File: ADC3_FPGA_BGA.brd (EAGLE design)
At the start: 40.4 x 44.4 mm, 120 parts, among them CON1 MEZZANINE_2X30, CON2 MEZZANINE_2X30, CON3 USB-C, IC1 ARTIX7-FTG256, IC2 3.3V, IC3 2.5V, IC4 MPM3811, IC5 MPM3804, IC6 EEPROM, IC7 93LC56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

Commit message: Create README.md
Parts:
- moved C1 32.8 mm to (23.5, 3.00)
- moved C10 32.8 mm to (17.5, 25.0)
- moved C11 32.8 mm to (2.00, 33.8)
- moved C12 32.8 mm to (21.0, 29.5)
- moved C13 32.8 mm to (23.0, 25.5)
- moved C14 32.8 mm to (17.0, 27.5)
- moved C15 32.8 mm to (21.0, 31.5)
- moved C16 32.8 mm to (20.0, 26.5)
- moved C17 32.8 mm to (23.0, 27.5)
- moved C18 32.8 mm to (19.5, 24.0)
- moved C19 32.8 mm to (13.0, 2.00)
- moved C2 32.8 mm to (17.0, 4.50)
- moved C20 32.8 mm to (7.00, 2.00)
- moved C21 32.8 mm to (22.0, 23.5)
- moved C22 32.8 mm to (19.0, 28.5)
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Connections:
- net DRAM_NRST: now also IC1.D8
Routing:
- net DRAM_NRST: track 1.92 -> 14.0 mm
- net +1V8: track 31.0 -> 31.6 mm
- net GND: vias 168 -> 180

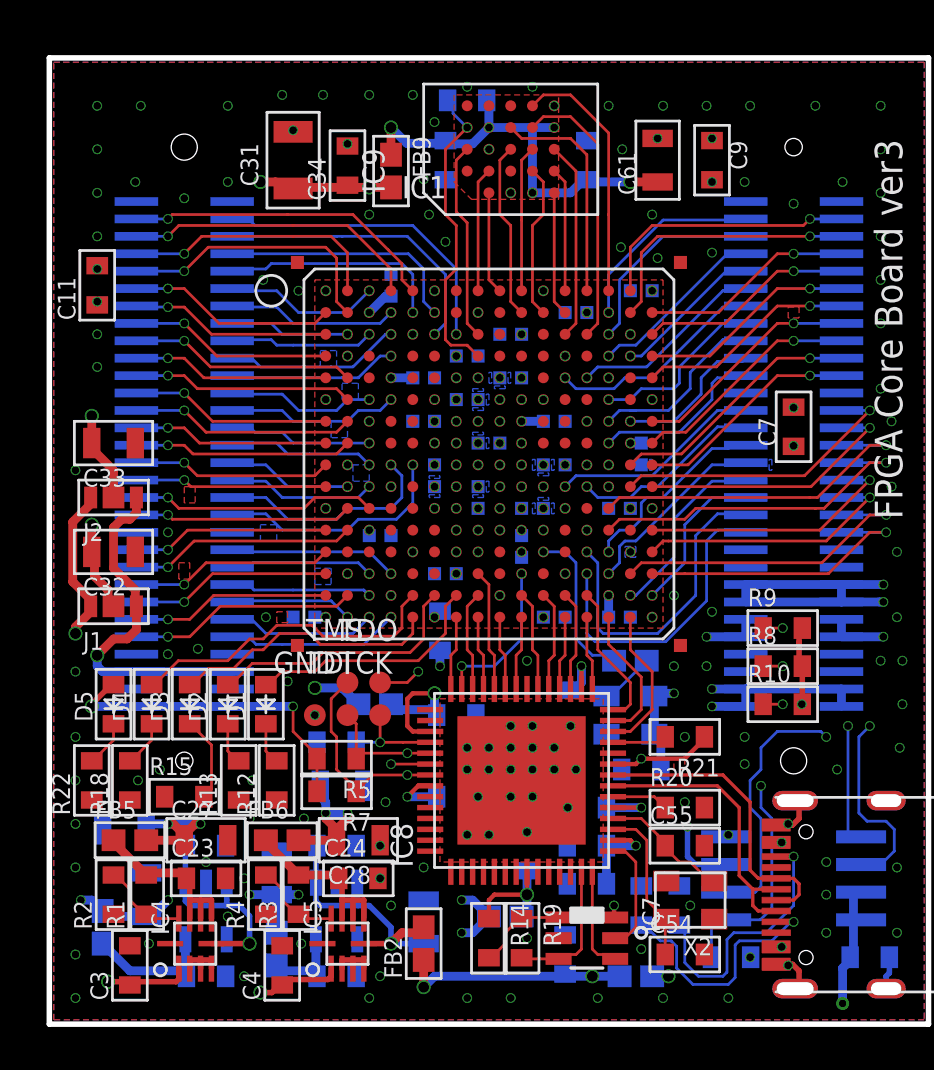
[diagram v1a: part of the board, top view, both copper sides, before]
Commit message: 長穴修正
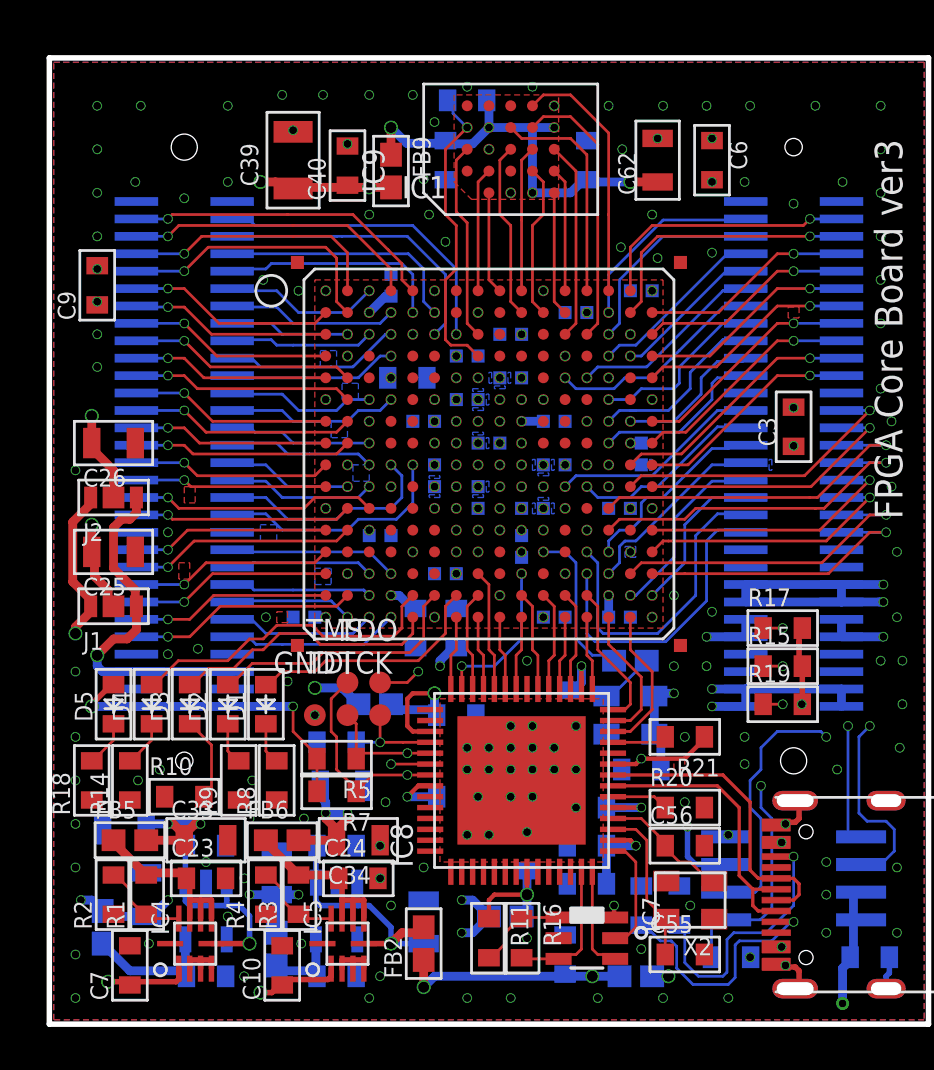
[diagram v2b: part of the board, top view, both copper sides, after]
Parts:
- added C62: 10u, my_rcl:2012
- C10, C21, C22: value 1u -> 10u; device my_rcl:1005 -> my_rcl:1608C
- C11, C8: value 4.7u -> 1u; device my_rcl:1608C -> my_rcl:1005
- C15, C16, C40: value 1u -> 0.1u; device my_rcl:1005 -> my_rcl:1608C
- C19, C20: value 10u -> 1u; device my_rcl:1608C -> my_rcl:1005
- C2, C29, C30: value 10u -> 4.7u; device my_rcl:2012 -> my_rcl:1608C
- C25, C26, C27, C28, C33: value 10u -> 47u
- C3: value 10u -> 4.7u
- C31: value 10u -> 1u; device my_rcl:3216 -> my_rcl:1005
- C32: value 10u -> 1u; device my_rcl:2012 -> my_rcl:1005
- C34: value 0.1u -> 47u; device my_rcl:1608C -> my_rcl:2012
- C37, C38: value 1u -> 47u; device my_rcl:1005 -> my_rcl:2012
- C39: value 1u -> 10u; device my_rcl:1005 -> my_rcl:3216
- C4: device my_rcl:1608C -> my_rcl:2012
- C48, C5: value 0.1u -> 1u; device my_rcl:1608C -> my_rcl:1005
- C54: value 22p -> 0.1u
- C56: value 10u -> 22p
- C57: value 0.1u -> 10u
- C59: value 1u -> 0.1u
- C6: value 0.1u -> 4.7u
- C61: value 10u -> 1u; device my_rcl:2012 -> my_rcl:1608C
- C7: value 4.7u -> 10u
- R10, R14, R8, R9: value 10k -> 1k
- R12, R13: value 1k -> 5.1k
- R15, R19, R22: value 1k -> 10k
- R16: value 5.1k -> 1k
- R17: value 5.1k -> 10k
- moved C3 39.3 mm to (34.0, 27.2)
- moved C7 39.3 mm to (3.50, 2.50)
- moved C6 39.2 mm to (30.2, 39.5), flipped to the top, turned to 270 degrees
- moved C59 31.5 mm to (24.5, 8.00), turned to 0 degrees
- moved C34 31.0 mm to (14.0, 8.25), turned to 0 degrees
- moved R22 30.5 mm to (31.1, 2.88), flipped to the bottom, turned to 180 degrees
- moved C22 29.1 mm to (7.00, 2.00)
- moved C9 28.8 mm to (2.00, 33.8), turned to 90 degrees
- moved R15 28.1 mm to (33.5, 16.2)
- moved R10 27.8 mm to (6.00, 10.2)
- moved C19 27.2 mm to (19.0, 28.5)
- moved C20 26.2 mm to (22.0, 23.5)
- moved R9 26.0 mm to (8.50, 11.0), turned to 90 degrees
- moved C15 24.8 mm to (13.0, 8.00), turned to 180 degrees
- moved C48 24.7 mm to (21.5, 21.8), turned to 90 degrees
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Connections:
- net +1V0: now also C11.1, C13.1, C17.1, C19.1, C2.1, C34.1, C38.1, C5.1; no longer C10.1, C12.1, C14.1, C16.1, C18.1, C22.1, C28.1, C30.1
- net +1V8: now also C12.1, C14.1, C18.1, C20.1, C3.1, C33.1, C37.1, C39.1, C41.1, C43.1, C45.1, C6.1; no longer C11.1, C13.1, C15.1, C17.1, C21.1, C27.1, C29.1, C31.1, C34.1, C42.1, C44.1, C7.1
- net +2V5: now also C28.1; no longer C26.1
- net +2V5_LDO: now also C22.1; no longer C20.1
- net +3V3: now also C27.1, C42.1, C44.1, C53.1, R15.2, R17.2, R19.2, R22.2; no longer C25.1, C41.1, C43.1, C45.1, R10.2, R11.2, R8.2, R9.2
- net +3V3_LDO: now also C21.1; no longer C19.1
- net DONE: now also R19.1; no longer R10.1
- net DRAM_+1V8: now also C62.1; no longer C59.1
- net FLASH_CS: now also R22.1; no longer R11.1
- net FT_+1V8: now also C59.1; no longer C56.1
- net FT_+3V3: now also C54.1, R11.1; no longer C53.1, R14.1
- net GND: now also C62.2, R10.1, R14.1, R8.1, R9.1; no longer R15.1, R16.1, R17.1, R22.1
- net INIT_B: now also R15.1; no longer R8.1
- net N$1: now also R18.2; no longer R22.2
- net N$10: now also R16.2; no longer R19.2
- net N$12: now also R11.2, R16.1; no longer R14.2, R19.1
- net N$13: now also C56.1; no longer C55.1
- net N$14: now also C55.1; no longer C54.1
- net N$2: now also R8.2; no longer R12.2
- net N$3: now also R9.2; no longer R13.2
- net N$4: now also R10.2; no longer R15.2
- net N$5: now also R14.2; no longer R18.2
- net N$6: now also R12.2; no longer R16.2
- net N$7: now also R13.2; no longer R17.2
- net PROGRAM_B: now also R17.1; no longer R9.1
- net VCCO34: now also C25.1, C29.1, C31.1; no longer C32.1, C37.1
- net VCCO35: now also C26.1, C30.1, C32.1; no longer C33.1, C38.1, C39.1
- net VIN_DCDC: now also C10.1, C15.1, C16.1, C7.1; no longer C2.1, C3.1, C5.1, C6.1
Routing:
- net VCCO34: track 4.91 -> 6.29 mm
- net VCCO35: track 6.47 -> 5.62 mm
- net +1V0: track 7.74 -> 8.27 mm
- added copper zone on layer 14, net GND
